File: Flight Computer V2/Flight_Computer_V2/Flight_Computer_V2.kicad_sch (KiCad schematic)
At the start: 0 parts

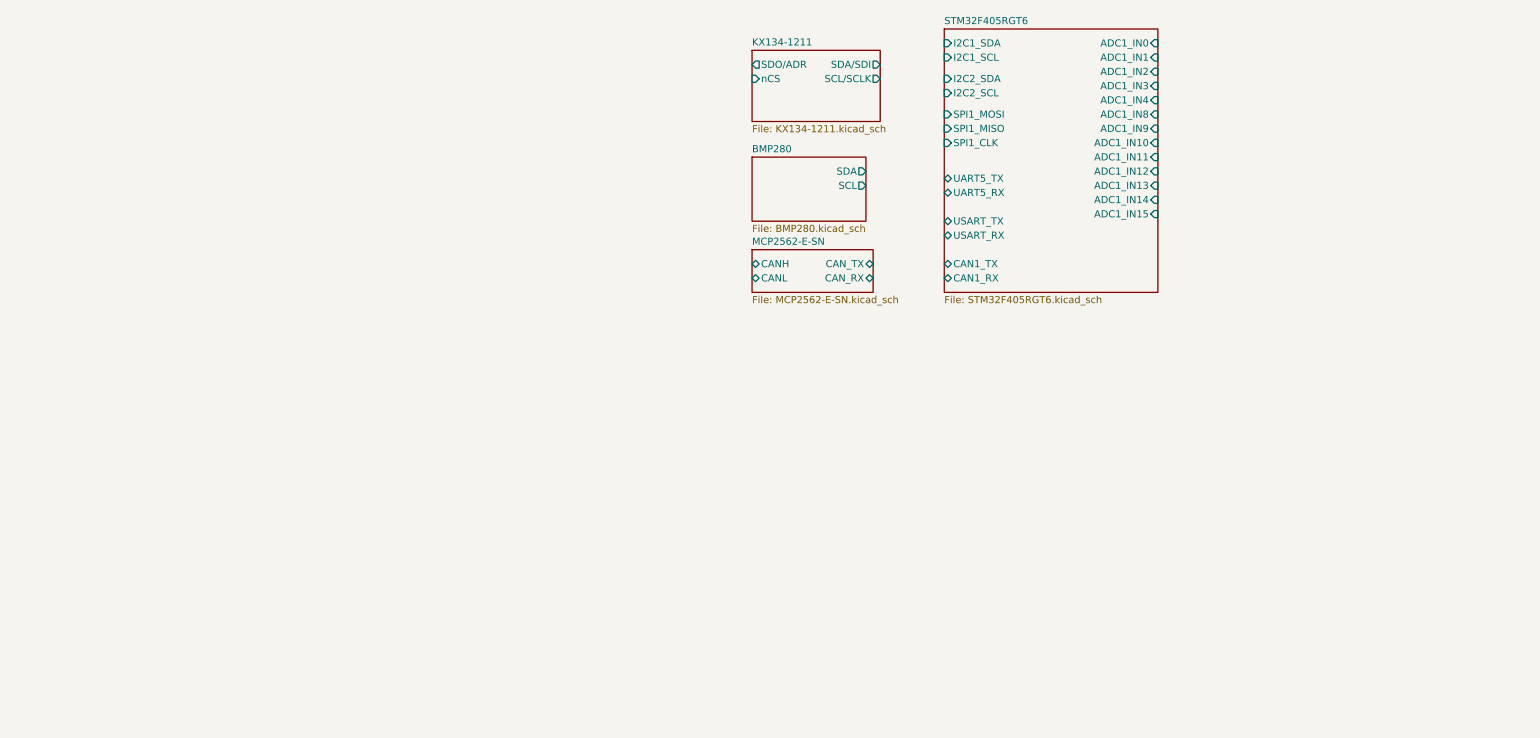
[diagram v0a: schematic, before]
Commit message: added more sensors to flight computer v2
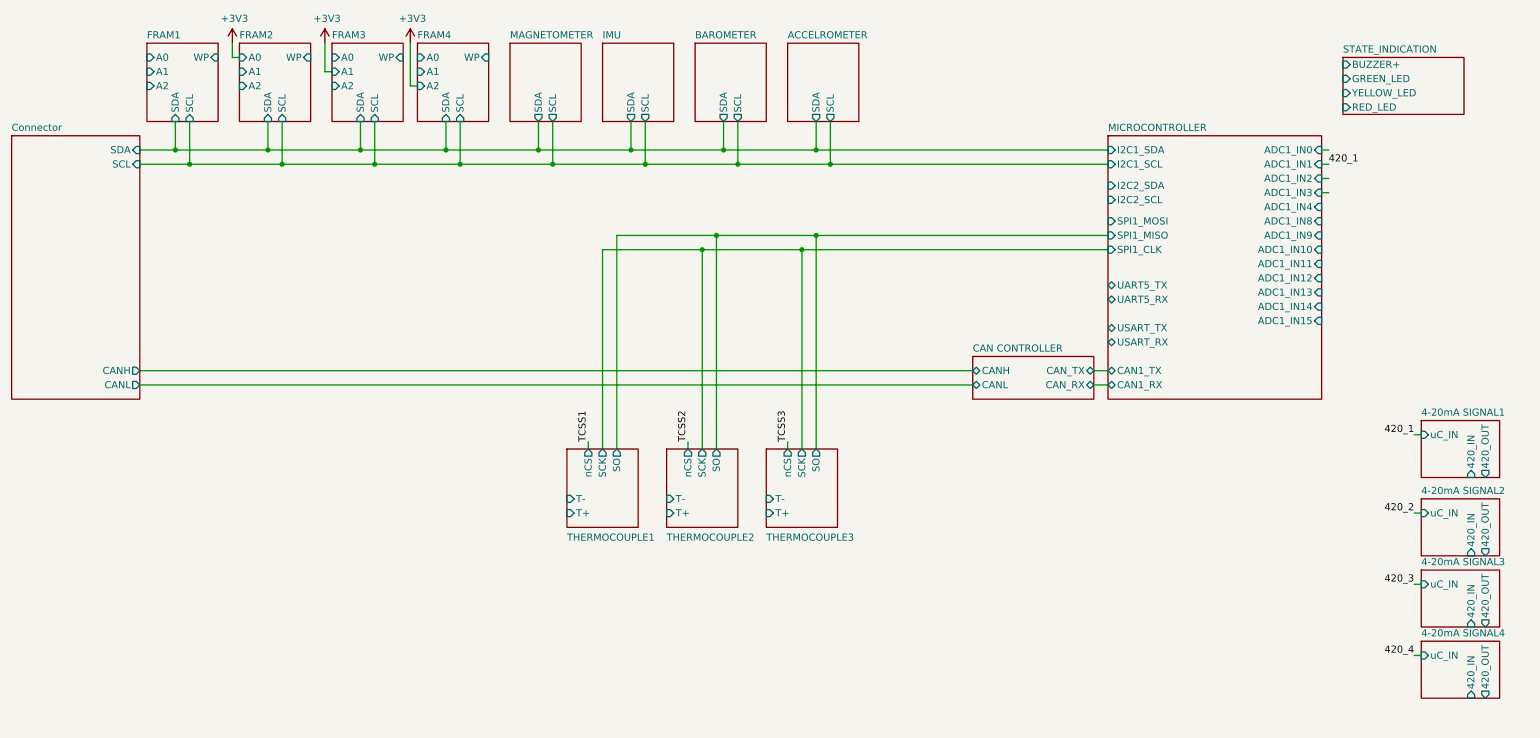
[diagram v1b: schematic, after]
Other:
- sheet BMP280 renamed BAROMETER
- sheet KX134-1211 renamed ACCELROMETER
- sheet MCP2562-E-SN renamed CAN CONTROLLER
- sheet STM32F405RGT6 renamed MICROCONTROLLER
- added sheet 4-20mA SIGNAL1 (4-20maSignal_sch.kicad_sch)
- added sheet 4-20mA SIGNAL2 (4-20maSignal_sch.kicad_sch)
- added sheet 4-20mA SIGNAL3 (4-20maSignal_sch.kicad_sch)
- added sheet 4-20mA SIGNAL4 (4-20maSignal_sch.kicad_sch)
- added sheet Connector (Connector.kicad_sch)
- added sheet FRAM1 (MB85RC256VPF-G-JNERE2.kicad_sch)
- added sheet FRAM2 (MB85RC256VPF-G-JNERE2.kicad_sch)
- added sheet FRAM3 (MB85RC256VPF-G-JNERE2.kicad_sch)
- added sheet FRAM4 (MB85RC256VPF-G-JNERE2.kicad_sch)
- added sheet IMU (BMI088.kicad_sch)
- added sheet MAGNETOMETER (MMC5603.kicad_sch)
- added sheet STATE_INDICATION (State_Indication.kicad_sch)
- added sheet THERMOCOUPLE1 (MAX31855KASA+T.kicad_sch)
- added sheet THERMOCOUPLE2 (MAX31855KASA+T.kicad_sch)
- added sheet THERMOCOUPLE3 (MAX31855KASA+T.kicad_sch)
- sheet ACCELROMETER ports: added SCL, SDA; removed SCL/SCLK, SDA/SDI, SDO/ADR, nCS

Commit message: more flgiht computer v2 updates
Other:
- sheet MICROCONTROLLER ports: added GPIO_OUTPUT1, GPIO_OUTPUT2; removed none

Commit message: finalized schematic, added datasheets, and pdf of schematic
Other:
- sheet 4-20mA SIGNAL1 ports: added none; removed 420_IN, 420_OUT
- sheet 4-20mA SIGNAL2 ports: added none; removed 420_IN, 420_OUT
- sheet 4-20mA SIGNAL3 ports: added none; removed 420_IN, 420_OUT
- sheet 4-20mA SIGNAL4 ports: added none; removed 420_IN, 420_OUT
- sheet MICROCONTROLLER ports: added none; removed I2C2_SCL, I2C2_SDA
- sheet THERMOCOUPLE1 ports: added none; removed T+, T-
- sheet THERMOCOUPLE2 ports: added none; removed T+, T-
- sheet THERMOCOUPLE3 ports: added none; removed T+, T-
- company: (none) -> By: Dylan Haussecker
- title: (none) -> Avionics Flight Computer
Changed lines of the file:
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@@
 (kicad_sch (version 20230121) (generator eeschema)
   (paper "A4")
+  (title_block
+    (title "Avionics Flight Computer")
+    (date "2023-09-04")
+    (rev "1.0")
+    (company "By: Dylan Haussecker")
+  )
   (junction (at 43.18 55.88) (diameter 0) (color 0 0 0 0)
   )
@@
     (stroke (width 0) (type default))
   )
-  (wire (pts (xy 241.3 111.76) (xy 242.57 111.76))
+  (wire (pts (xy 241.3 113.03) (xy 242.57 113.03))
     (stroke (width 0) (type default))
   )
@@
     (effects (font (size 1.27 1.27)) (justify right bottom))
   )
-  (label "420_1" (at 241.3 111.76 180) (fields_autoplaced)
+  (label "420_1" (at 241.3 113.03 180) (fields_autoplaced)
     (effects (font (size 1.27 1.27)) (justify right bottom))
   )
@@
       (effects (font (size 1.27 1.27)) (justify left top) hide)
     )
-    (pin "T-" input (at 113.03 118.11 180)
-      (effects (font (size 1.27 1.27)) (justify left))
-    )
-    (pin "T+" input (at 113.03 120.65 180)
-      (effects (font (size 1.27 1.27)) (justify left))
-    )
     (pin "SO" output (at 121.92 109.22 90)
       (effects (font (size 1.27 1.27)) (justify right))
@@
       (effects (font (size 1.27 1.27)) (justify right))
     )
-    (pin "I2C2_SCL" input (at 209.55 64.77 180)
-      (effects (font (size 1.27 1.27)) (justify left))
-    )
     (pin "I2C1_SDA" input (at 209.55 55.88 180)
       (effects (font (size 1.27 1.27)) (justify left))
@@
     )
     (pin "I2C1_SCL" input (at 209.55 58.42 180)
-      (effects (font (size 1.27 1.27)) (justify left))
-    )
-    (pin "I2C2_SDA" input (at 209.55 62.23 180)
       (effects (font (size 1.27 1.27)) (justify left))
     )
@@
       (effects (font (size 1.27 1.27)) (justify left top) hide)
     )
-    (pin "T-" input (at 148.59 118.11 180)
-      (effects (font (size 1.27 1.27)) (justify left))
-    )
-    (pin "T+" input (at 148.59 120.65 180)
-      (effects (font (size 1.27 1.27)) (justify left))
-    )
     (pin "SO" output (at 157.48 109.22 90)
       (effects (font (size 1.27 1.27)) (justify right))
@@
       (effects (font (size 1.27 1.27)) (justify left top) hide)
     )
-    (pin "420_OUT" output (at 254 133.35 270)
-      (effects (font (size 1.27 1.27)) (justify left))
-    )
     (pin "uC_IN" input (at 242.57 125.73 180)
-      (effects (font (size 1.27 1.27)) (justify left))
-    )
-    (pin "420_IN" input (at 251.46 133.35 270)
       (effects (font (size 1.27 1.27)) (justify left))
     )
@@
       (effects (font (size 1.27 1.27)) (justify left top) hide)
     )
-    (pin "420_OUT" output (at 254 146.05 270)
-      (effects (font (size 1.27 1.27)) (justify left))
-    )
     (pin "uC_IN" input (at 242.57 138.43 180)
-      (effects (font (size 1.27 1.27)) (justify left))
-    )
-    (pin "420_IN" input (at 251.46 146.05 270)
       (effects (font (size 1.27 1.27)) (justify left))
     )
@@
     )
   )
-  (sheet (at 242.57 109.22) (size 13.97 10.16) (fields_autoplaced)
+  (sheet (at 242.57 110.49) (size 13.97 10.16) (fields_autoplaced)
     (stroke (width 0.1524) (type solid))
     (fill (color 176 244 255 1.0000))
-    (property "Sheetname" "4-20mA SIGNAL1" (at 242.57 108.5084 0)
-      (effects (font (size 1.27 1.27)) (justify left bottom))
-    )
-    (property "Sheetfile" "4-20maSignal_sch.kicad_sch" (at 242.57 119.9646 0)
-      (effects (font (size 1.27 1.27)) (justify left top) hide)
-    )
-    (pin "420_OUT" output (at 254 119.38 270)
-      (effects (font (size 1.27 1.27)) (justify left))
-    )
-    (pin "uC_IN" input (at 242.57 111.76 180)
-      (effects (font (size 1.27 1.27)) (justify left))
-    )
-    (pin "420_IN" input (at 251.46 119.38 270)
+    (property "Sheetname" "4-20mA SIGNAL1" (at 242.57 109.7784 0)
+      (effects (font (size 1.27 1.27)) (justify left bottom))
+    )
+    (property "Sheetfile" "4-20maSignal_sch.kicad_sch" (at 242.57 121.2346 0)
+      (effects (font (size 1.27 1.27)) (justify left top) hide)
+    )
+    (pin "uC_IN" input (at 242.57 113.03 180)
       (effects (font (size 1.27 1.27)) (justify left))
     )
@@
       (effects (font (size 1.27 1.27)) (justify left top) hide)
     )
-    (pin "420_OUT" output (at 254 158.75 270)
-      (effects (font (size 1.27 1.27)) (justify left))
-    )
     (pin "uC_IN" input (at 242.57 151.13 180)
-      (effects (font (size 1.27 1.27)) (justify left))
-    )
-    (pin "420_IN" input (at 251.46 158.75 270)
       (effects (font (size 1.27 1.27)) (justify left))
     )
@@
       (effects (font (size 1.27 1.27)) (justify left top) hide)
     )
-    (pin "T-" input (at 130.81 118.11 180)
-      (effects (font (size 1.27 1.27)) (justify left))
-    )
-    (pin "T+" input (at 130.81 120.65 180)
-      (effects (font (size 1.27 1.27)) (justify left))
-    )
     (pin "SO" output (at 139.7 109.22 90)

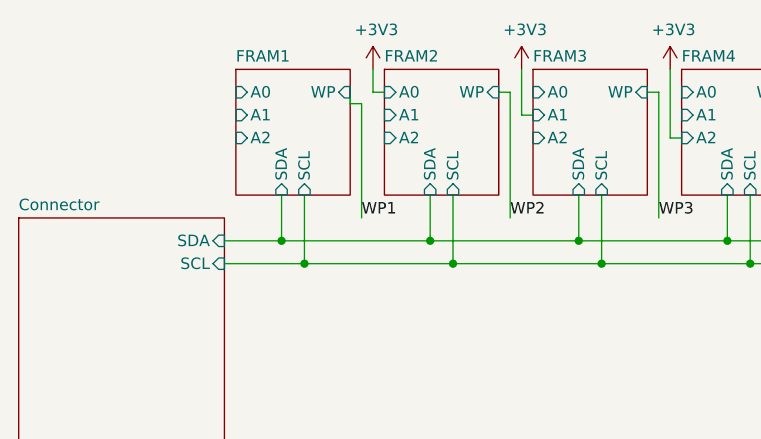
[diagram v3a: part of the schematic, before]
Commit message: changed new flight computer scl resistors
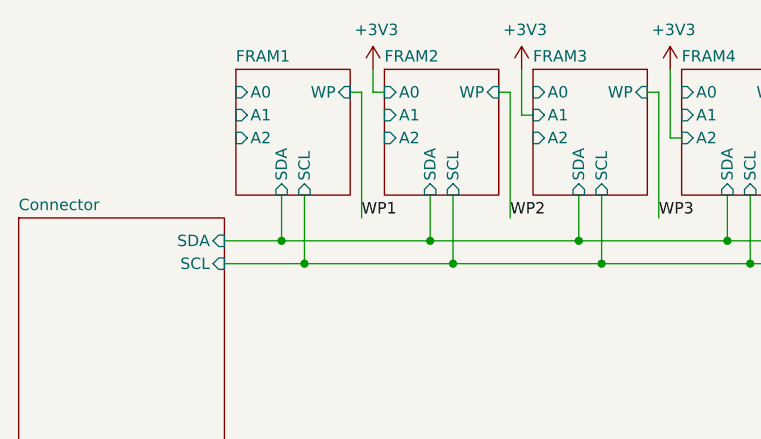
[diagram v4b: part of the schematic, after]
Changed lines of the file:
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@@
     (stroke (width 0) (type default))
   )
-  (wire (pts (xy 52.07 40.64) (xy 52.07 53.34))
+  (wire (pts (xy 52.07 39.37) (xy 52.07 53.34))
     (stroke (width 0) (type default))
   )
@@
   )
   (wire (pts (xy 128.27 50.8) (xy 128.27 58.42))
-    (stroke (width 0) (type default))
-  )
-  (wire (pts (xy 50.8 40.64) (xy 50.8 39.37))
     (stroke (width 0) (type default))
   )
@@
     (stroke (width 0) (type default))
   )
-  (wire (pts (xy 50.8 40.64) (xy 52.07 40.64))
+  (wire (pts (xy 50.8 39.37) (xy 52.07 39.37))
     (stroke (width 0) (type default))
   )
